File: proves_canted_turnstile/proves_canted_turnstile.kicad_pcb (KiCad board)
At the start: 4 copper layers, 100 x 100 mm, 44 parts, among them J1 Conn_Coaxial, J10 WDT Disable Jumper, J11 DEBUG, J12 USB_C_Receptacle_USB2.0_16P, J3 Battery Charge Bypass, J6 FC Reset Jumper, J7 FC USB Bootselect Jumper, J8 USB_C_Receptacle_USB2.0_16P, J9 DF11-4DP-2DSA, U1 QBA-07+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

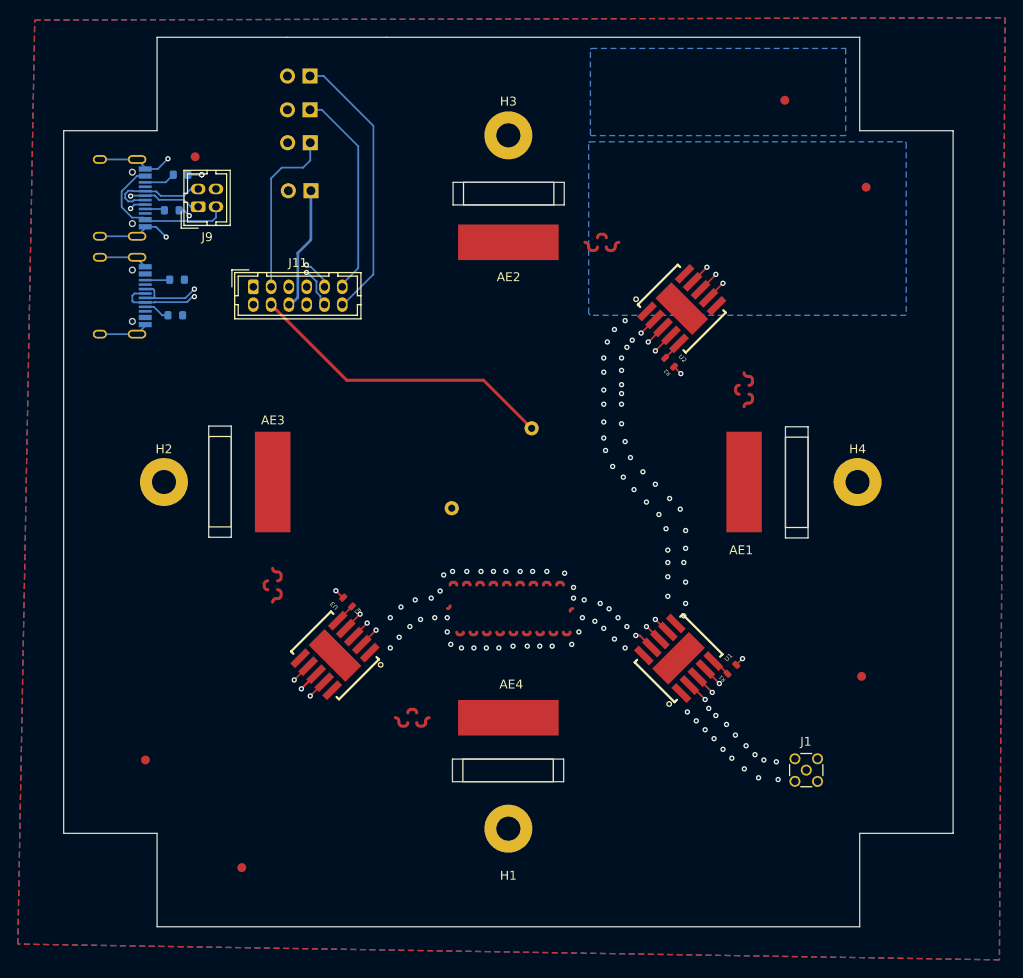
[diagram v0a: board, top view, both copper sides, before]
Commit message: Update proves_canted_turnstile.kicad_pcb
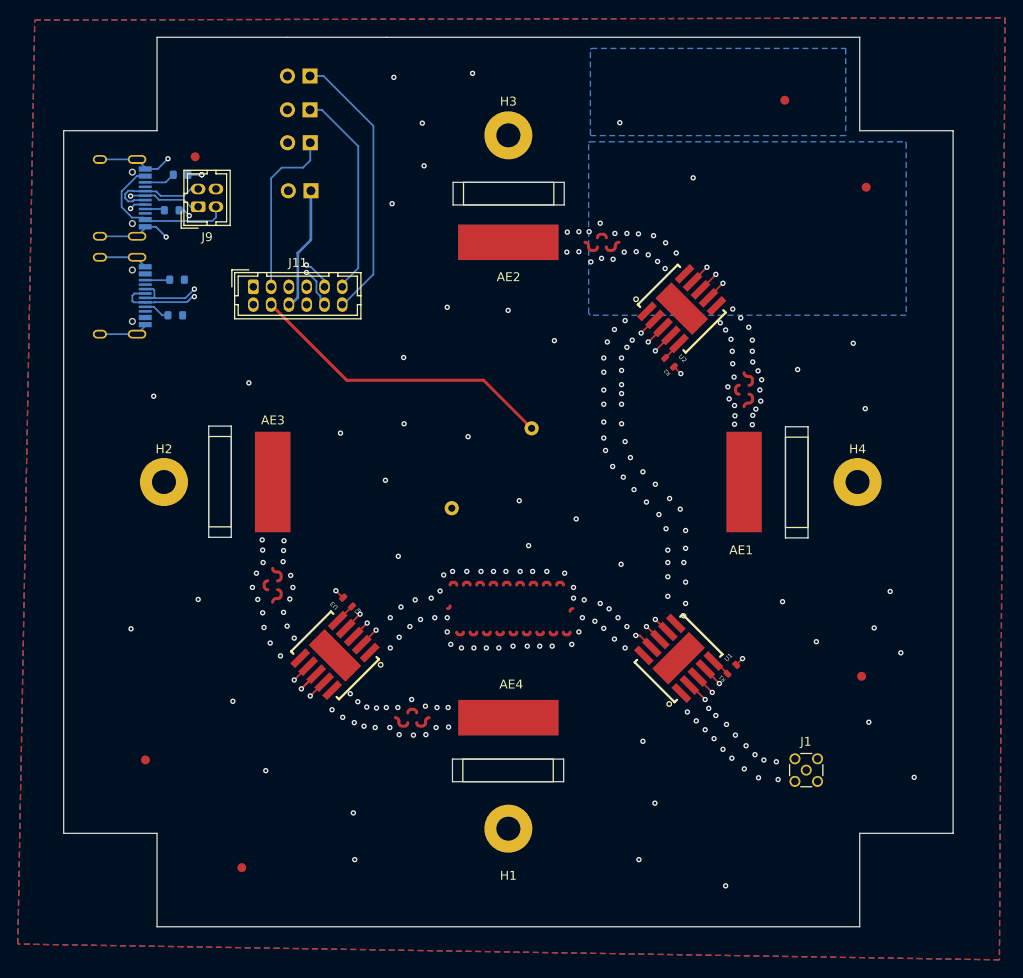
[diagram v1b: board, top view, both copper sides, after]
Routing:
- net GND: vias 128 -> 254

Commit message: changed burnwire resistor position
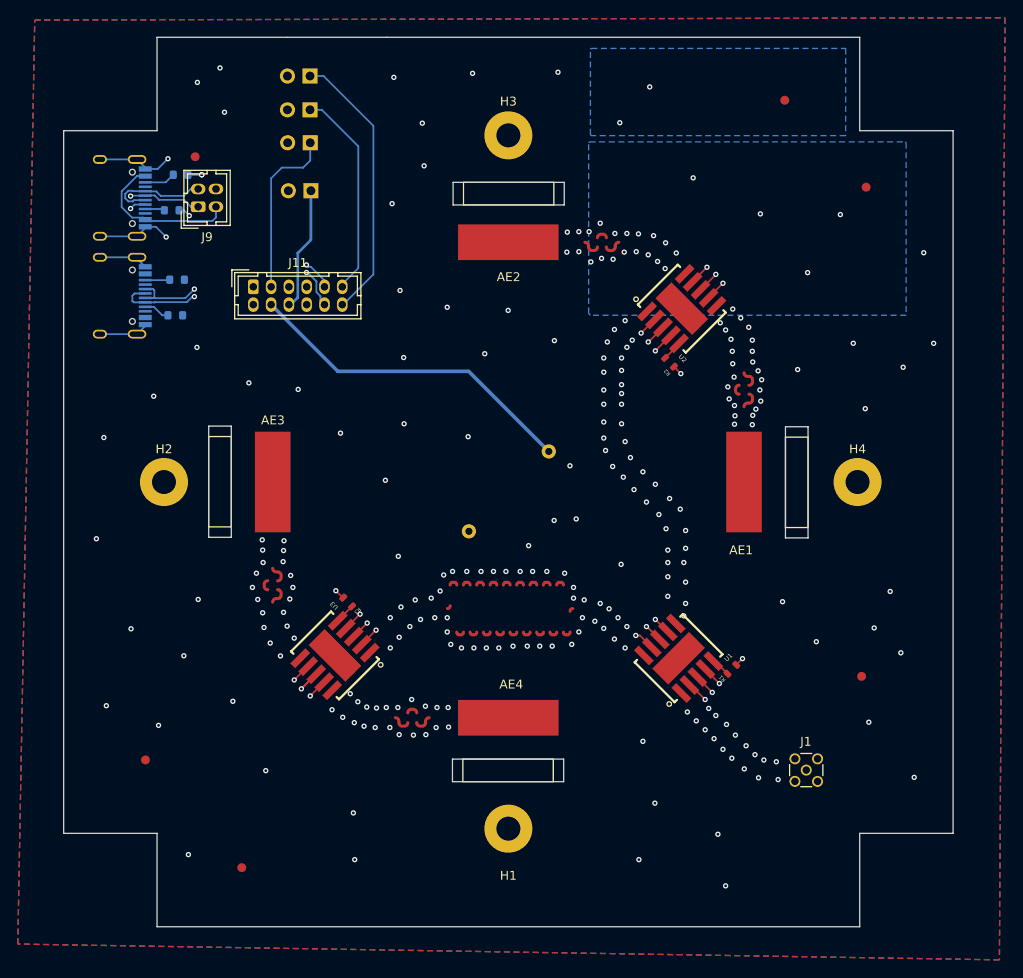
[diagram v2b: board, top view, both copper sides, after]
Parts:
- moved R4 7.50 mm to (143.7, 83.5)
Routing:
- net BURN: track 35.1 -> 38.1 mm
- net GND: vias 254 -> 277

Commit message: Update proves_canted_turnstile.kicad_pcb
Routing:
- net GND: vias 277 -> 290
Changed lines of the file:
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@@
-		)
-	)
-	(dimension
-		(type orthogonal)
-		(layer "Dwgs.User")
-		(pts
-			(xy 143.675 43.5692) (xy 143.675 121.5192)
-		)
-		(height -67.2972)
-		(orientation 1)
-		(format
-			(prefix "")
-			(suffix "")
-			(units 3)
-			(units_format 0)
-			(precision 4)
-			(suppress_zeroes yes)
-		)
-		(style
-			(thickness 0.1)
-			(arrow_length 1.27)
-			(text_position_mode 0)
-			(arrow_direction outward)
-			(extension_height 0.58642)
-			(extension_offset 0.5)
-			(keep_text_aligned yes)
-		)
-		(gr_text "77.95"
-			(at 75.2278 82.5442 90)
-			(layer "Dwgs.User")
-			(effects
-				(font
-					(size 1 1)
-					(thickness 0.15)
-				)
-			)
-		)
-	)
-	(dimension
-		(type orthogonal)
-		(layer "Dwgs.User")
-		(pts
-			(xy 104.9546 82.547) (xy 182.9346 82.547)
-		)
-		(height -62.2016)
-		(orientation 0)
-		(format
-			(prefix "")
-			(suffix "")
-			(units 3)
-			(units_format 0)
-			(precision 4)
-			(suppress_zeroes yes)
-		)
-		(style
-			(thickness 0.1)
-			(arrow_length 1.27)
-			(text_position_mode 0)
-			(arrow_direction outward)
-			(extension_height 0.58642)
-			(extension_offset 0.5)
-			(keep_text_aligned yes)
-		)
-		(gr_text "77.98"
-			(at 143.9446 19.1954 0)
-			(layer "Dwgs.User")
-			(effects
-				(font
-					(size 1 1)
-					(thickness 0.15)
-				)
-			)
 		)
 	)
@@
 	)
 	(via
+		(at 162.814 102.362)
+		(size 0.6)
+		(drill 0.3)
+		(layers "F.Cu" "B.Cu")
+		(net 7)
+	)
+	(via
 		(at 156.4 72.6)
 		(size 0.6)
@@
 	)
 	(via
+		(at 135.5344 82.423)
+		(size 0.6)
+		(drill 0.3)
+		(layers "F.Cu" "B.Cu")
+		(free yes)
+		(net 7)
+	)
+	(via
 		(at 108.712 37.6174)
 		(size 0.6)
@@
 	)
 	(via
+		(at 136.5758 72.644)
+		(size 0.6)
+		(drill 0.3)
+		(layers "F.Cu" "B.Cu")
+		(free yes)
+		(net 7)
+	)
+	(via
 		(at 174 116)
 		(size 0.6)
@@
 	)
 	(via
+		(at 124.333 113.7158)
+		(size 0.6)
+		(drill 0.3)
+		(layers "F.Cu" "B.Cu")
+		(free yes)
+		(net 7)
+	)
+	(via
 		(at 131.6 96.6)
 		(size 0.6)
@@
 	)
 	(via
+		(at 130.937 44.0182)
+		(size 0.6)
+		(drill 0.3)
+		(layers "F.Cu" "B.Cu")
+		(free yes)
+		(net 7)
+	)
+	(via
 		(at 167 108.8)
 		(size 0.6)
@@
 	)
 	(via
+		(at 146.558 73.7616)
+		(size 0.6)
+		(drill 0.3)
+		(layers "F.Cu" "B.Cu")
+		(free yes)
+		(net 7)
+	)
+	(via
 		(at 137.4 92.6)
 		(size 0.6)
@@
 	)
 	(via
+		(at 163.17 63.052)
+		(size 0.6)
+		(drill 0.3)
+		(layers "F.Cu" "B.Cu")
+		(net 7)
+	)
+	(via
 		(at 154 53.45)
 		(size 0.6)
@@
 	)
 	(via
+		(at 150.1648 62.9158)
+		(size 0.6)
+		(drill 0.3)
+		(layers "F.Cu" "B.Cu")
+		(free yes)
+		(net 7)
+	)
+	(via
 		(at 148.6 101)
 		(size 0.6)
@@
 	)
 	(via
+		(at 124.1799 102.0421)
+		(size 0.6)
+		(drill 0.3)
+		(layers "F.Cu" "B.Cu")
+		(net 7)
+	)
+	(via
 		(at 181.0004 52.4764)
 		(size 0.6)
@@
 	)
 	(via
+		(at 103.505 92.8624)
+		(size 0.6)
+		(drill 0.3)
+		(layers "F.Cu" "B.Cu")
+		(free yes)
+		(net 7)
+	)
+	(via
 		(at 177.3174 59.0042)
 		(size 0.6)
@@
 	)
 	(via
+		(at 127.0508 36.2458)
+		(size 0.6)
+		(drill 0.3)
+		(layers "F.Cu" "B.Cu")
+		(free yes)
+		(net 7)
+	)
+	(via
 		(at 168.7 66.5)
 		(size 0.6)
@@
 	)
 	(via
+		(at 132.8674 117.6528)
+		(size 0.6)
+		(drill 0.3)
+		(layers "F.Cu" "B.Cu")
+		(free yes)
+		(net 7)
+	)
+	(via
 		(at 168.8 113.6)
 		(size 0.6)
@@
 		(size 0.6)
 		(drill 0.3)
+		(layers "F.Cu" "B.Cu")
+		(free yes)
+		(net 7)
+	)
+	(via
+		(at 152.8064 120.015)
+		(size 0.6)
+		(drill 0.3)

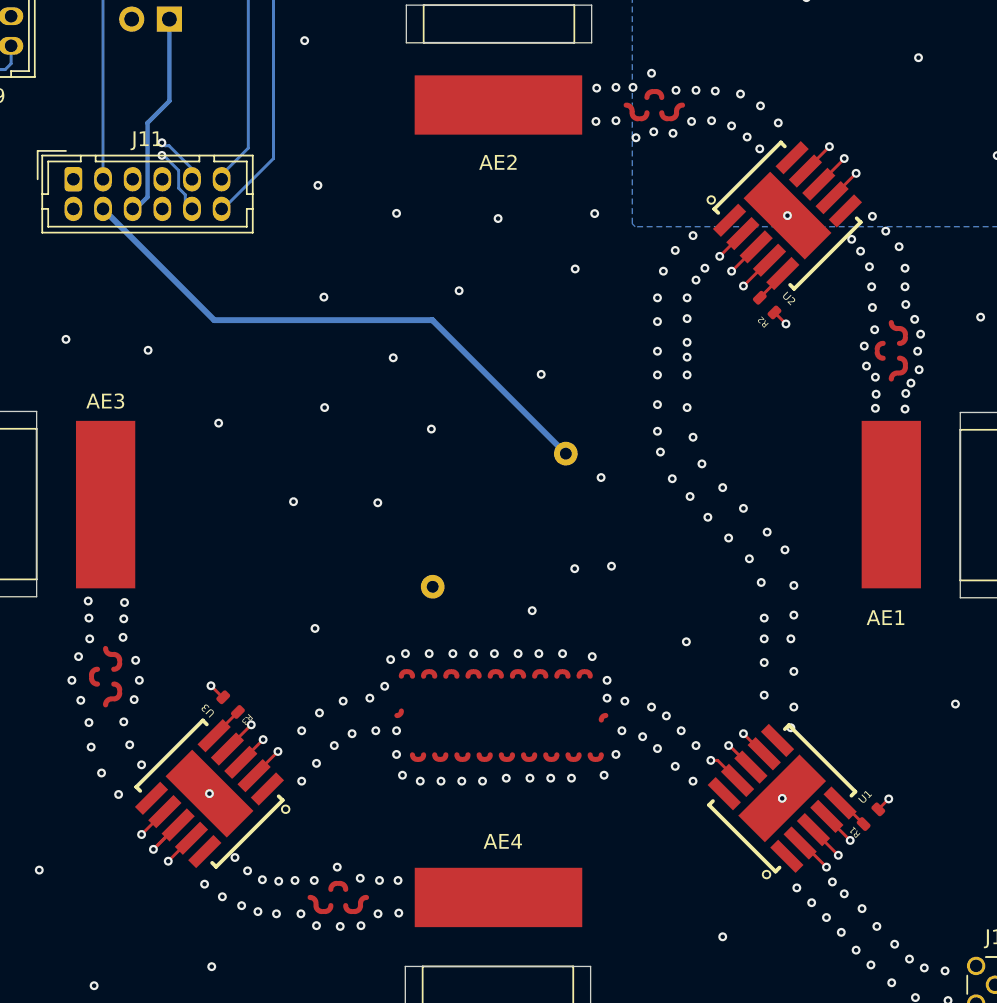
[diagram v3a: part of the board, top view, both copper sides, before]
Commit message: updated impedance of rf traces to be single ended coplanar
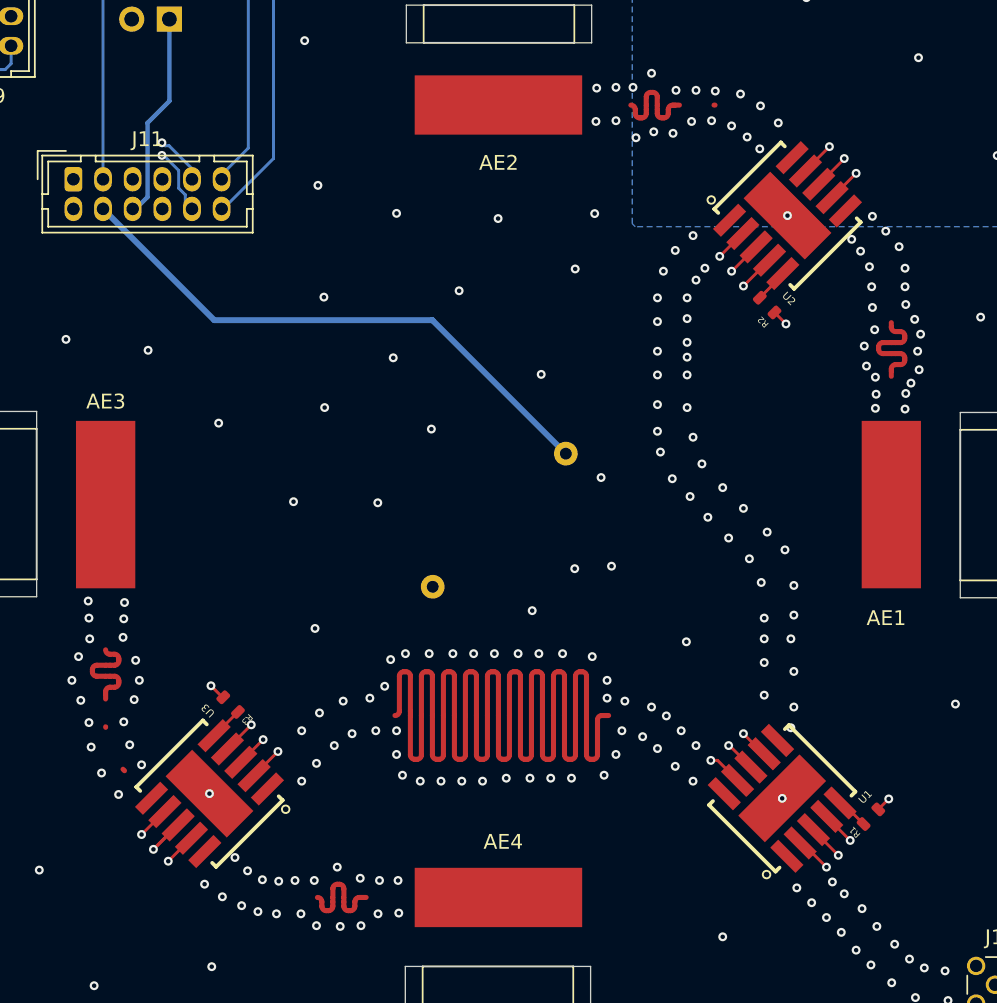
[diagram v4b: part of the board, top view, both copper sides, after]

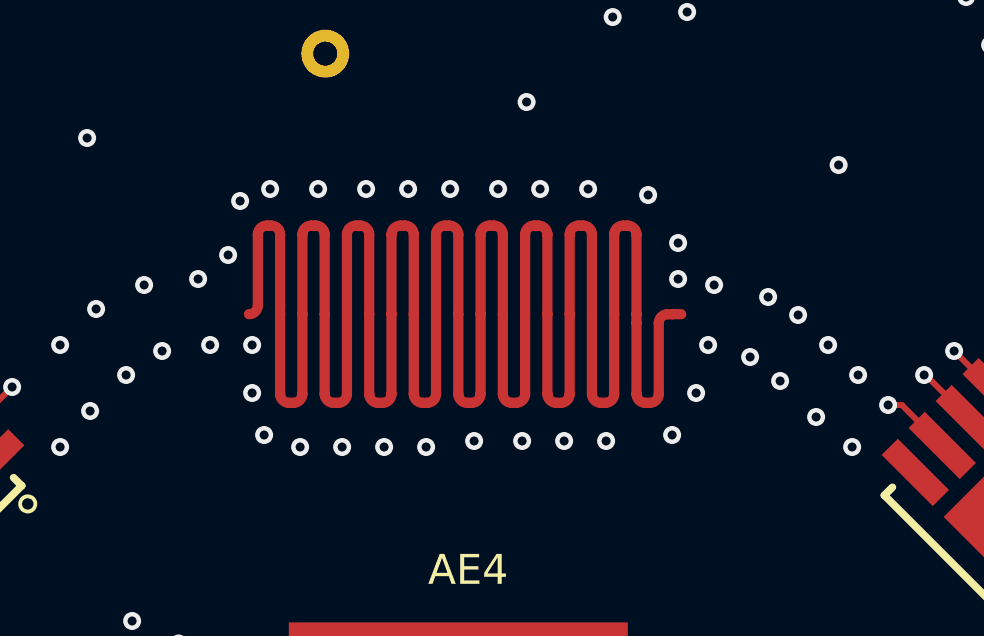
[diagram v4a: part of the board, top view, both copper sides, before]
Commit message: updated 90 degree phase shift trace length
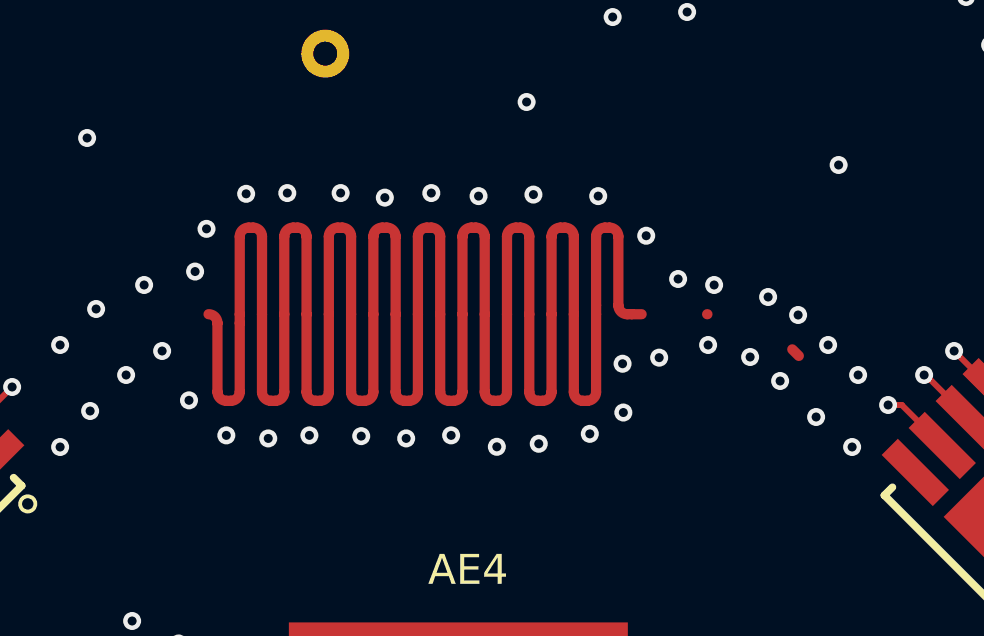
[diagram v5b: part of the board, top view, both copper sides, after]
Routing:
- net /UHF-SHORT+1/4WAVE: track 135.7 -> 133.3 mm
- net GND: vias 290 -> 287
